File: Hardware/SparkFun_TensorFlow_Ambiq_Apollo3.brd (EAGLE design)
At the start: 40 x 40 mm, 96 parts, among them J5 CORTEX_DEBUG, J7 CAMERA-HIMAX, U2 LIS2DH12, U3 1.8V, U5 ARTEMIS_MODULESMD, Y2 32.768kHz

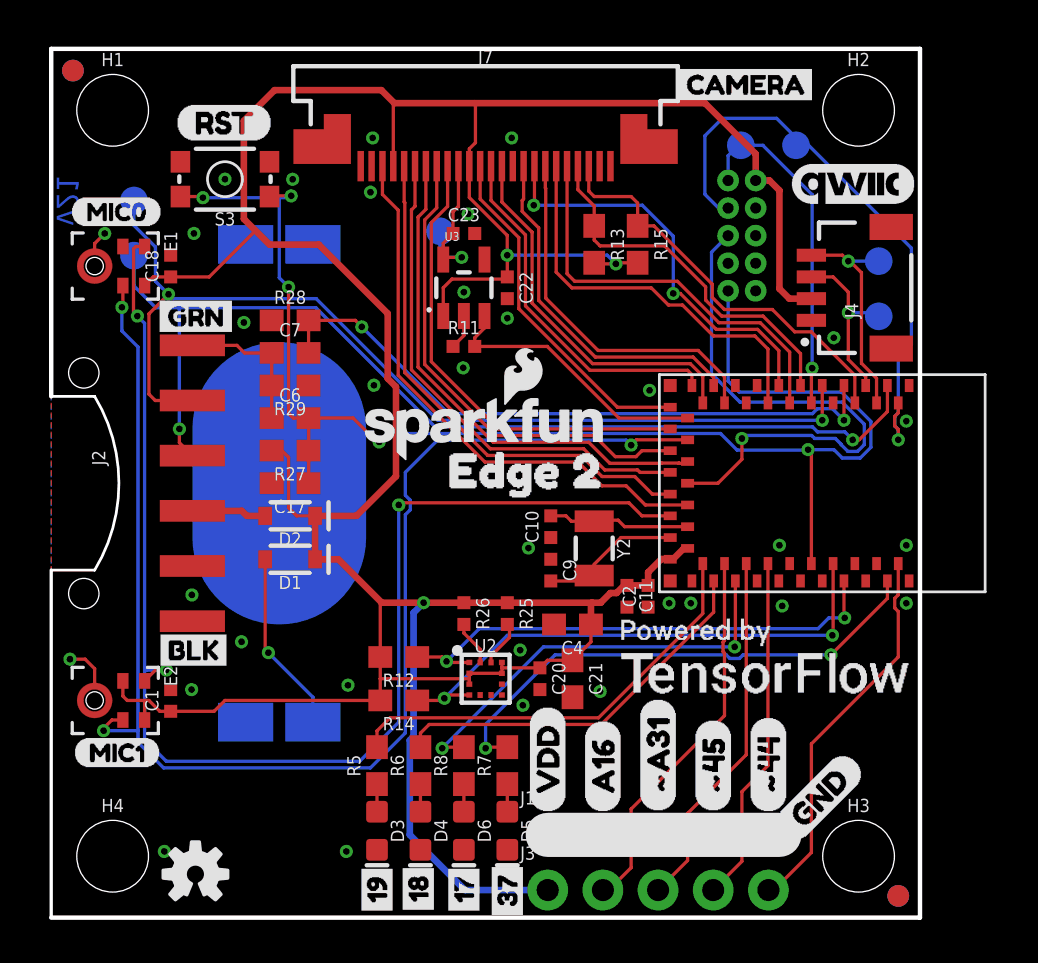
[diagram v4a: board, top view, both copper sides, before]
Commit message: Move cap to avoid silk
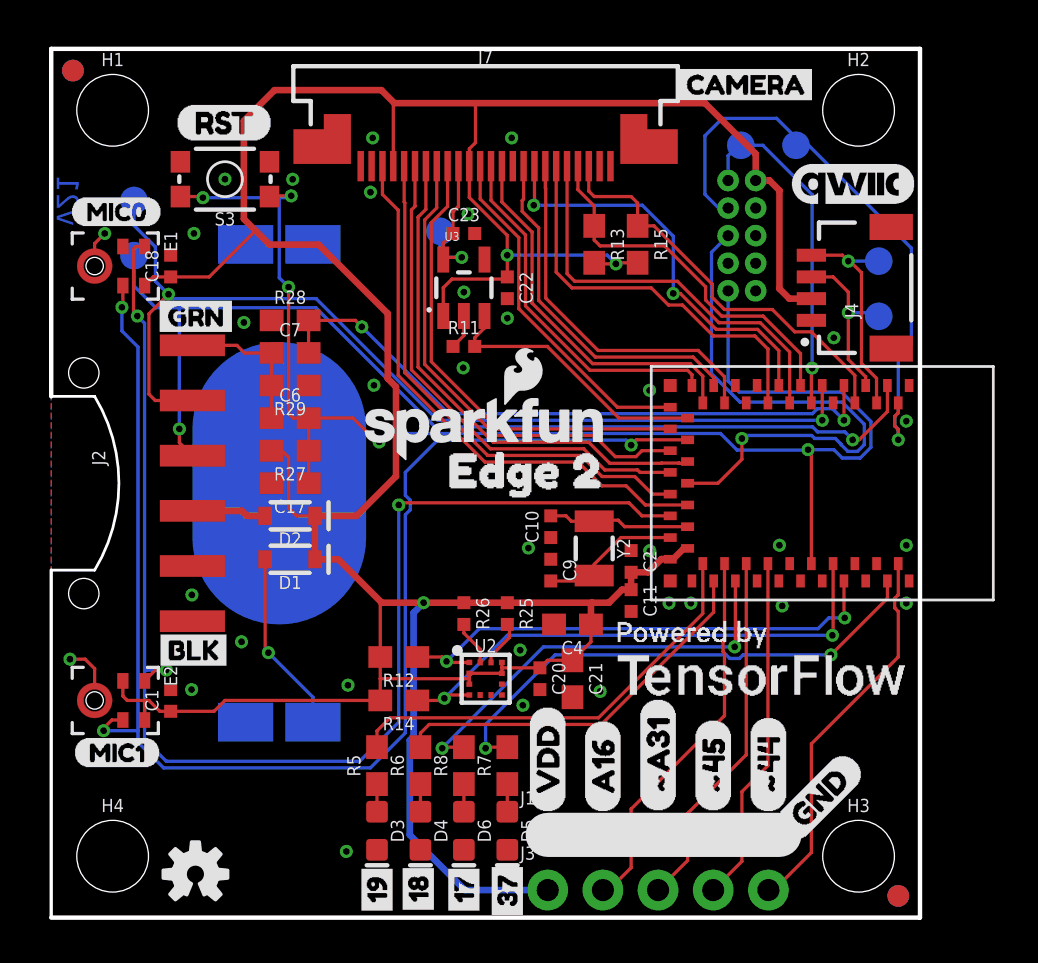
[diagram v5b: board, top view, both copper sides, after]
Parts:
- U5: device Testing:ARTEMIS_FP -> SparkFun-IC-Microcontroller:ARTEMIS_FP
- moved C2 1.78 mm to (26.7, 16.4), turned to 270 degrees
- moved C11 0.28 mm to (26.7, 14.6)
- moved U$21 0.19 mm to (32.6, 12.2)
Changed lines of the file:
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@@
 <layer number="47" name="Measures" color="7" fill="1" visible="no" active="yes"/>
 <layer number="48" name="Document" color="7" fill="1" visible="no" active="yes"/>
-<layer number="49" name="Reference" color="7" fill="1" visible="yes" active="yes"/>
+<layer number="49" name="Reference" color="7" fill="1" visible="no" active="yes"/>
 <layer number="50" name="dxf" color="7" fill="1" visible="no" active="yes"/>
 <layer number="51" name="tDocu" color="6" fill="1" visible="yes" active="yes"/>
@@
 <element name="U$19" library="Labels" package="QWIIC_COPYRIGHT_SMALL" value="" x="36.9" y="33.8" smashed="yes"/>
 <element name="U$20" library="buzzard_labels" package="CAMERA3" value="" x="28.448" y="38.354" smashed="yes"/>
-<element name="U$21" library="PoweredBy_TF#jpg" package="POWEREDBY_TF#JPG" value="" x="32.766" y="12.3" smashed="yes"/>
+<element name="U$21" library="PoweredBy_TF#jpg" package="POWEREDBY_TF#JPG" value="" x="32.6" y="12.2" smashed="yes"/>
 <element name="U$1" library="buzzard_labels" package="MIC00" value="" x="0.9" y="32.5" smashed="yes"/>
 <element name="TP1" library="SparkFun-Connectors" package="PAD.03X.05" value="" x="34.29" y="35.56" smashed="yes" rot="MR0"/>
@@
 <element name="U$29" library="SparkFun-Aesthetics" package="SFE_LOGO_NAME_.1" value="" x="24.64" y="36" smashed="yes" rot="MR0"/>
 <element name="U$30" library="SparkFun-Aesthetics" package="OSHW-LOGO-S" value="" x="2.64" y="7" smashed="yes" rot="MR0"/>
-<element name="U5" library="Testing" package="ARTEMIS_FP" value="ARTEMIS_MODULESMD" x="35" y="20" smashed="yes"/>
+<element name="U5" library="SparkFun-IC-Microcontroller" package="ARTEMIS_FP" value="ARTEMIS_MODULESMD" x="35" y="20" smashed="yes">
+<attribute name="PROD_ID" value="SUB-14415" x="35" y="20" size="1.778" layer="27" display="off"/>
+</element>
 <element name="E1" library="SparkFun-Sensors" package="SPH0641LM4H-1_MICROPHONE" value="SPH0641LM4H-1" x="3" y="30" smashed="yes" rot="R270">
 <attribute name="NAME" x="5.2" y="31.6" size="0.6" layer="25" font="vector" rot="R270"/>
@@
 <attribute name="VALUE" x="34.2638" y="33.2288" size="0.6096" layer="28" font="vector" ratio="20" rot="MR270"/>
 </element>
-<element name="C2" library="SparkFun-Capacitors" package="0402-TIGHT" value="0.1uF" x="27.481" y="14.797" smashed="yes" rot="R90">
-<attribute name="NAME" x="26.919" y="14.797" size="0.6096" layer="25" font="vector" ratio="20" rot="R90" align="bottom-center"/>
-<attribute name="PROD_ID" value="CAP-12416" x="27.481" y="12.257" size="1.778" layer="27" font="vector" ratio="15" rot="R90" display="off"/>
-<attribute name="VALUE" x="28.043" y="14.797" size="0.6096" layer="27" font="vector" ratio="20" rot="R90" align="top-center"/>
+<element name="C2" library="SparkFun-Capacitors" package="0402-TIGHT" value="0.1uF" x="26.7" y="16.4" smashed="yes" rot="R270">
+<attribute name="NAME" x="27.262" y="16.4" size="0.6096" layer="25" font="vector" ratio="20" rot="R270" align="bottom-center"/>
+<attribute name="PROD_ID" value="CAP-12416" x="26.7" y="18.94" size="1.778" layer="27" font="vector" ratio="15" rot="R270" display="off"/>
+<attribute name="VALUE" x="26.138" y="16.4" size="0.6096" layer="27" font="vector" ratio="20" rot="R270" align="top-center"/>
 </element>
 <element name="C4" library="SparkFun-Capacitors" package="0603" value="10uF" x="24" y="13.5" smashed="yes" rot="R180">
@@
 <attribute name="VALUE" x="24" y="14.262" size="0.6096" layer="27" font="vector" ratio="20" rot="R180" align="top-center"/>
 </element>
-<element name="C11" library="SparkFun-Capacitors" package="0402-TIGHT" value="1.0uF" x="26.508" y="14.797" smashed="yes" rot="R270">
-<attribute name="NAME" x="27.07" y="14.797" size="0.6096" layer="25" font="vector" ratio="20" rot="R270" align="bottom-center"/>
-<attribute name="PROD_ID" value="CAP-12417" x="22.698" y="13.527" size="1.778" layer="27" font="vector" ratio="15" rot="R270" display="off"/>
-<attribute name="VALUE" x="25.946" y="14.797" size="0.6096" layer="27" font="vector" ratio="20" rot="R270" align="top-center"/>
+<element name="C11" library="SparkFun-Capacitors" package="0402-TIGHT" value="1.0uF" x="26.7" y="14.6" smashed="yes" rot="R270">
+<attribute name="NAME" x="27.262" y="14.6" size="0.6096" layer="25" font="vector" ratio="20" rot="R270" align="bottom-center"/>
+<attribute name="PROD_ID" value="CAP-12417" x="22.89" y="13.33" size="1.778" layer="27" font="vector" ratio="15" rot="R270" display="off"/>
+<attribute name="VALUE" x="26.138" y="14.6" size="0.6096" layer="27" font="vector" ratio="20" rot="R270" align="top-center"/>
 </element>
 <element name="E2" library="SparkFun-Sensors" package="SPH0641LM4H-1_MICROPHONE" value="SPH0641LM4H-1" x="3" y="10" smashed="yes" rot="R270">
@@
 <wire x1="13.218" y1="16.5" x2="15.218" y2="14.5" width="0.3048" layer="1"/>
 <wire x1="19" y1="14.5" x2="21" y2="14.5" width="0.3048" layer="1"/>
-<wire x1="25.3" y1="14.5" x2="24.9" y2="14.5" width="0.3048" layer="1"/>
 <wire x1="24.9" y1="14.5" x2="21" y2="14.5" width="0.3048" layer="1"/>
 <wire x1="28.49" y1="16.51" x2="28.5" y2="16.5" width="0.3048" layer="1"/>
@@
 <wire x1="16.6858" y1="8.34698125" x2="16.6858" y2="14.0408" width="0.3048" layer="16"/>
 <wire x1="16.6858" y1="14.0408" x2="17.145" y2="14.5" width="0.3048" layer="16"/>
-<wire x1="27.481" y1="15.297" x2="26.508" y2="15.297" width="0.3048" layer="1"/>
-<wire x1="25.3" y1="14.5" x2="25.7452" y2="14.9452" width="0.3048" layer="1"/>
-<wire x1="25.7452" y1="14.9452" x2="26.02625" y2="14.9452" width="0.3048" layer="1"/>
-<wire x1="26.37805" y1="15.297" x2="26.508" y2="15.297" width="0.3048" layer="1"/>
-<wire x1="26.02625" y1="14.9452" x2="26.37805" y2="15.297" width="0.3048" layer="1"/>
-<wire x1="27.481" y1="15.297" x2="27.481" y2="15.9" width="0.3048" layer="1"/>
+<wire x1="26.7" y1="15.9" x2="26.7" y2="15.1" width="0.3048" layer="1"/>
+<wire x1="26.796" y1="15.1" x2="26.7" y2="15.1" width="0.3048" layer="1"/>
+<wire x1="24.9" y1="14.5" x2="25.68105" y2="14.5" width="0.3048" layer="1"/>
+<wire x1="26.28105" y1="15.1" x2="26.7" y2="15.1" width="0.3048" layer="1"/>
+<wire x1="25.68105" y1="14.5" x2="26.28105" y2="15.1" width="0.3048" layer="1"/>
+<wire x1="26.7" y1="15.9" x2="27.481" y2="15.9" width="0.3048" layer="1"/>
 <wire x1="27.481" y1="15.9" x2="28.091" y2="16.51" width="0.3048" layer="1"/>
 <wire x1="28.091" y1="16.51" x2="28.49" y2="16.51" width="0.3048" layer="1"/>
@@
 <contactref element="C1" pad="2"/>
 <via x="36.0334" y="26.7" extent="1-16" drill="0.3048"/>
-<via x="5.207" y="3.048" extent="1-16" drill="0.3048"/>
 <polygon width="0.1524" layer="1" isolate="0.1524">
 <vertex x="0" y="40"/>
@@
 <via x="21.717" y="9.779" extent="1-16" drill="0.3048"/>
 <via x="25.273" y="10.414" extent="1-16" drill="0.3048"/>
-<wire x1="5.255" y1="3" x2="5.207" y2="3.048" width="0.1524" layer="1"/>
 <via x="21.59" y="12.319" extent="1-16" drill="0.3048"/>
 <via x="19" y="28.8" extent="1-16" drill="0.3048"/>
@@
 <wire x1="1.562" y1="11.9" x2="0.863" y2="11.9" width="0.1524" layer="1"/>
 <wire x1="2" y1="11.462" x2="1.562" y2="11.9" width="0.1524" layer="1"/>
+<via x="27.559" y="16.891" extent="1-16" drill="0.3048"/>
 </signal>
 <signal name="SWDCK">
@@
 <wire x1="17.67374375" y1="22.5952" x2="12.18894375" y2="28.08" width="0.1524" layer="16"/>
 <wire x1="12.18894375" y1="28.08" x2="5.9" y2="28.08" width="0.1524" layer="16"/>
-<wire x1="3.81" y1="30.08" x2="3.81" y2="30.4" width="0.1524" layer="16"/>
-<wire x1="3.81" y1="30.4" x2="3.81" y2="30.48" width="0.1524" layer="16"/>
 <wire x1="5.9" y1="28.08" x2="4.82" y2="28.08" width="0.1524" layer="16"/>
-<wire x1="3.81" y1="29.09" x2="3.81" y2="30.08" width="0.1524" layer="16"/>
+<wire x1="3.81" y1="29.09" x2="3.81" y2="30.48" width="0.1524" layer="16"/>
 <wire x1="4.82" y1="28.08" x2="3.81" y2="29.09" width="0.1524" layer="16"/>
 </signal>
@@
 <wire x1="36.42094375" y1="23.7334" x2="36.09765625" y2="23.7334" width="0.1524" layer="16"/>
 <wire x1="36.09765625" y1="23.7334" x2="36.09285625" y2="23.7382" width="0.1524" layer="16"/>
-<wire x1="36.09285625" y1="23.7382" x2="33" y2="23.7382" width="0.1524" layer="16"/>
-<wire x1="33" y1="23.7382" x2="31.70745625" y2="23.7382" width="0.1524" layer="16"/>
+<wire x1="36.09285625" y1="23.7382" x2="31.70745625" y2="23.7382" width="0.1524" layer="16"/>
 <wire x1="31.70745625" y1="23.7382" x2="30.4" y2="25.04565625" width="0.1524" layer="16"/>
 <wire x1="30.4" y1="30.635" x2="31.165" y2="31.4" width="0.1524" layer="16"/>
 <wire x1="30.4" y1="25.04565625" x2="30.4" y2="30.635" width="0.1524" layer="16"/>
-<wire x1="33" y1="23.7382" x2="33" y2="23.7382" width="0.1524" layer="16"/>
 </signal>
 <signal name="N$2">

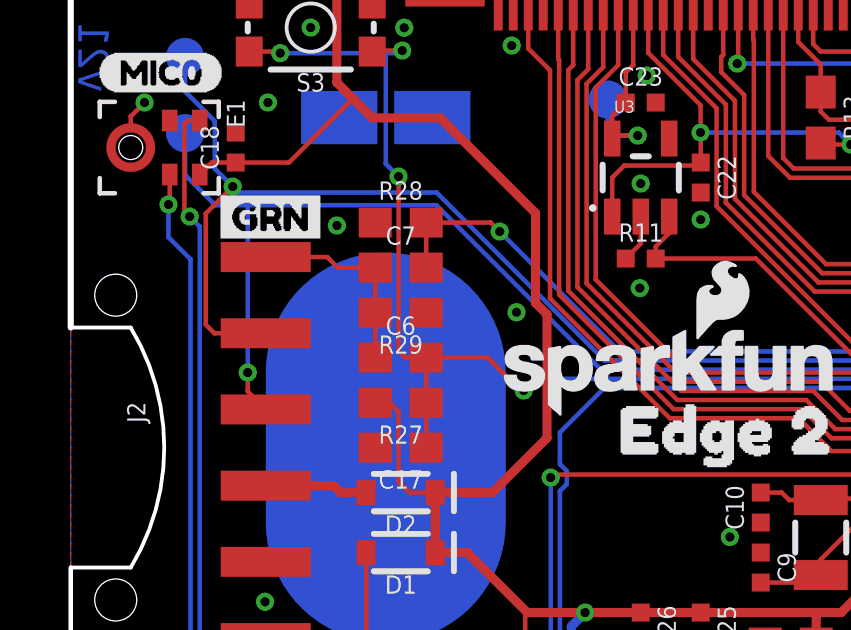
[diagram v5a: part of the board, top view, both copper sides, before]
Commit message: Change bootload circuit to use 0.1uF/220k standards.
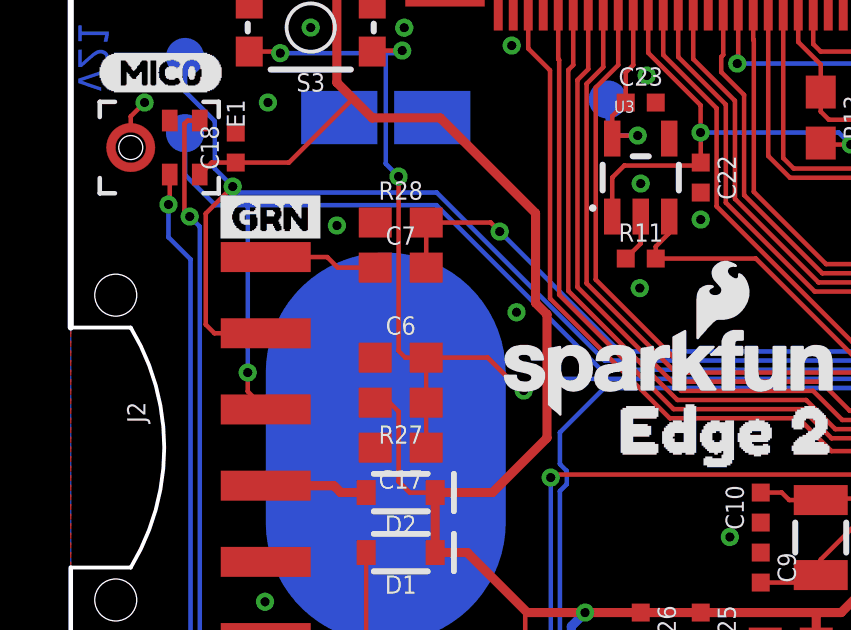
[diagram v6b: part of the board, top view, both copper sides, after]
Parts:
- removed R29: 100k, SparkFun-Resistors:0603
- C7: value 2.2uF -> 0.1uF
- R28: value 10k -> 220k
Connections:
- net !DTR: no longer R29.2
- net GND: no longer R29.1
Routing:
- net !DTR: track 6.79 -> 3.79 mm
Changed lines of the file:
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@@
 <attribute name="VALUE" x="11" y="22.238" size="0.6096" layer="27" font="vector" ratio="20" align="top-center"/>
 </element>
-<element name="R28" library="SparkFun-Resistors" package="0603" value="10k" x="11" y="27.5" smashed="yes">
+<element name="R28" library="SparkFun-Resistors" package="0603" value="220k" x="11" y="27.5" smashed="yes">
 <attribute name="NAME" x="11" y="28.262" size="0.6096" layer="25" font="vector" ratio="20" align="bottom-center"/>
-<attribute name="PROD_ID" value="RES-00824" x="11" y="23.69" size="1.778" layer="27" font="vector" ratio="15" display="off"/>
-<attribute name="VALUE" x="11" y="26.738" size="0.6096" layer="27" font="vector" ratio="20" align="top-center"/>
-</element>
-<element name="C7" library="SparkFun-Capacitors" package="0603" value="2.2uF" x="11" y="26" smashed="yes">
+<attribute name="PROD_ID" value="RES-08969" x="11" y="23.69" size="1.778" layer="27" font="vector" ratio="15" display="off"/>
+<attribute name="VALUE" value="220k" x="11" y="26.738" size="0.6096" layer="27" font="vector" ratio="20" align="top-center"/>
+</element>
+<element name="C7" library="SparkFun-Capacitors" package="0603" value="0.1uF" x="11" y="26" smashed="yes">
 <attribute name="NAME" x="11" y="26.762" size="0.6096" layer="25" font="vector" ratio="20" align="bottom-center"/>
-<attribute name="PROD_ID" value="CAP-07888" x="11" y="14.57" size="1.778" layer="27" font="vector" ratio="15" display="off"/>
-<attribute name="VALUE" x="11" y="25.238" size="0.6096" layer="27" font="vector" ratio="20" align="top-center"/>
-</element>
-<element name="R29" library="SparkFun-Resistors" package="0603" value="100k" x="11" y="24.5" smashed="yes" rot="R180">
-<attribute name="NAME" x="11" y="23.738" size="0.6096" layer="25" font="vector" ratio="20" rot="R180" align="bottom-center"/>
-<attribute name="PROD_ID" value="RES-07828" x="14.81" y="35.93" size="1.778" layer="27" font="vector" ratio="15" rot="R180" display="off"/>
-<attribute name="VALUE" x="11" y="25.262" size="0.6096" layer="27" font="vector" ratio="20" rot="R180" align="top-center"/>
+<attribute name="PROD_ID" value="CAP-00810" x="11" y="14.57" size="1.778" layer="27" font="vector" ratio="15" display="off"/>
+<attribute name="VALUE" value="0.1uF" x="11" y="25.238" size="0.6096" layer="27" font="vector" ratio="20" align="top-center"/>
 </element>
 <element name="C17" library="SparkFun-Capacitors" package="0603" value="1nF" x="11" y="20" smashed="yes" rot="R180">
@@
 <contactref element="J4" pad="1"/>
 <contactref element="R28" pad="1"/>
-<contactref element="R29" pad="1"/>
 <contactref element="C17" pad="2"/>
 <contactref element="S3" pad="1"/>
@@
 <contactref element="J2" pad="1"/>
 <contactref element="C7" pad="1"/>
-<contactref element="R29" pad="2"/>
 <contactref element="C6" pad="1"/>
 <wire x1="6.5" y1="26.35" x2="8.55" y2="26.35" width="0.1524" layer="1"/>
 <wire x1="8.55" y1="26.35" x2="8.9" y2="26" width="0.1524" layer="1"/>
 <wire x1="8.9" y1="26" x2="10.15" y2="26" width="0.1524" layer="1"/>
-<wire x1="10.15" y1="26" x2="10.15" y2="24.5" width="0.1524" layer="1"/>
-<wire x1="10.15" y1="24.5" x2="10.15" y2="23" width="0.1524" layer="1"/>
+<wire x1="10.15" y1="26" x2="10.15" y2="23" width="0" layer="19" extent="1-1"/>
 </signal>
 <signal name="V_BATT">
